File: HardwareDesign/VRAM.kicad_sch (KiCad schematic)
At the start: 8 parts, among them U801 IDT7134, U802 IDT7134, U803 GAL22V10, U804 74HCT574

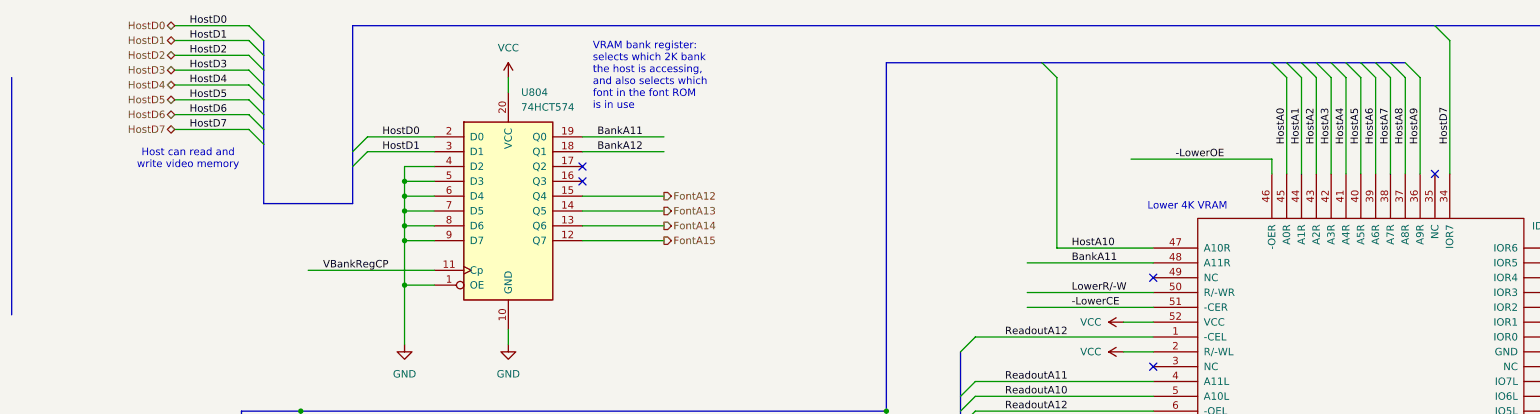
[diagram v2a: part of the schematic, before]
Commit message: the host needs to write all bits of bank reg
The high 4 bits of the VRAM bank register are used
for selecting the font, but this is only possible
if the bank register's inputs are actually
connected to the host data bus.
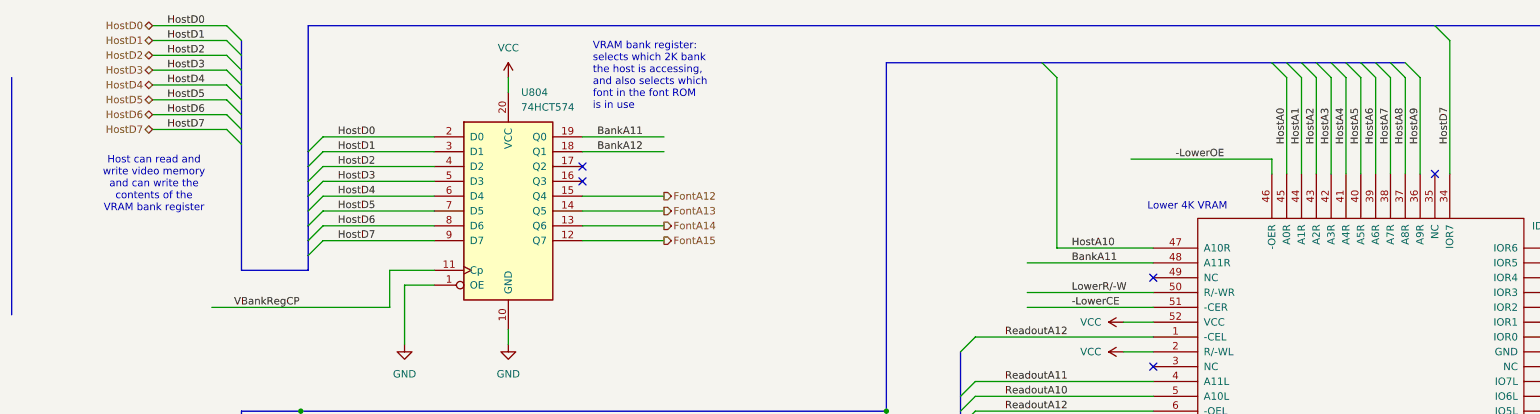
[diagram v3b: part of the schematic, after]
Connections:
- net GND: no longer U804.4 (D2), U804.5 (D3), U804.6 (D4), U804.7 (D5), U804.8 (D6), U804.9 (D7)
- net HostD2: now also U804.4 (D2)
- net HostD3: now also U804.5 (D3)
- net HostD4: now also U804.6 (D4)
- net HostD5: now also U804.7 (D5)
- net HostD6: now also U804.8 (D6)
- net HostD7: now also U804.9 (D7)
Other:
- note added: "Host can read and write video memory and can write the contents of the VRAM bank register"
- note removed: "Host can read and write video memory"

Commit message: make bank register a 74ACT574
But, a 74HCT574 should also work, since this is the
host side, which is far slower than the display
controller side.
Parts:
- U804: value 74HCT574 -> 74ACT574
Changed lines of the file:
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@@
 			)
 		)
-		(property "Value" "74HCT574"
+		(property "Value" "74ACT574"
 			(at 88.5541 30.48 0)
 			(effects

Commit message: use 74ALS and 74HCT parts where possible
The '574 implementing the VRAM module's bank register
can be a 74HCT574 because it's only driven by
(relatively slow) signals from the host system.

Changed the Readout module to use 74ALS273 rather than
74ACT273 for the row begin address register.

Changed the Pixgen module to use 74ALS574 rather than
74ACT574 for the character and attribute registers.
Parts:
- U804: value 74ACT574 -> 74HCT574
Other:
- note added: "Note that this doesn't need to be a high-speed part since it's only driven by signals from the host system."
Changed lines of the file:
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@@
+		)
+	)
+	(text "Note that this doesn't need to be\na high-speed part since it's\nonly driven by signals from the\nhost system."
+		(exclude_from_sim no)
+		(at 97.282 60.706 0)
+		(effects
+			(font
+				(size 1.27 1.27)
+			)
+			(justify left)
 		)
 	)
@@
 			)
 		)
-		(property "Value" "74ACT574"
+		(property "Value" "74HCT574"
 			(at 88.5541 30.48 0)
 			(effects
